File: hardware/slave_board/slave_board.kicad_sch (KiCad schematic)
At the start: 0 parts

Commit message: feat(hw): complete Root and Power_Stage schematic routing
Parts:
- added J1: RJ45_Shielded, symbol Connector:RJ45_Shielded
- added J2: Barrel_Jack_MountingPin, symbol Connector:Barrel_Jack_MountingPin
- added J3: Screw_Terminal_01x04, symbol Connector:Screw_Terminal_01x04
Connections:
- new net +12V: J2.1
- new net +3.3V: J1.3
- new net 1W_DATA: J1.8
- new net ADC_ALERT: J1.7
- new net FAN_PWM: J1.6
- new net GND: J1.2, J1.SH, J2.2
- new net I2C_SCL: J1.5
- new net I2C_SDA: J1.4
- new net LOAD_FORCE_+: J3.1 (Pin_1)
- new net LOAD_FORCE_-: J3.4 (Pin_4)
- new net LOAD_SENSE_+: J3.2 (Pin_2)
- new net LOAD_SENSE_-: J3.3 (Pin_3)
- new net PWM_IN: J1.1
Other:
- added sheet Power_Stage (power_stage.kicad_sch)
- added sheet Telemetry (telemetry.kicad_sch)

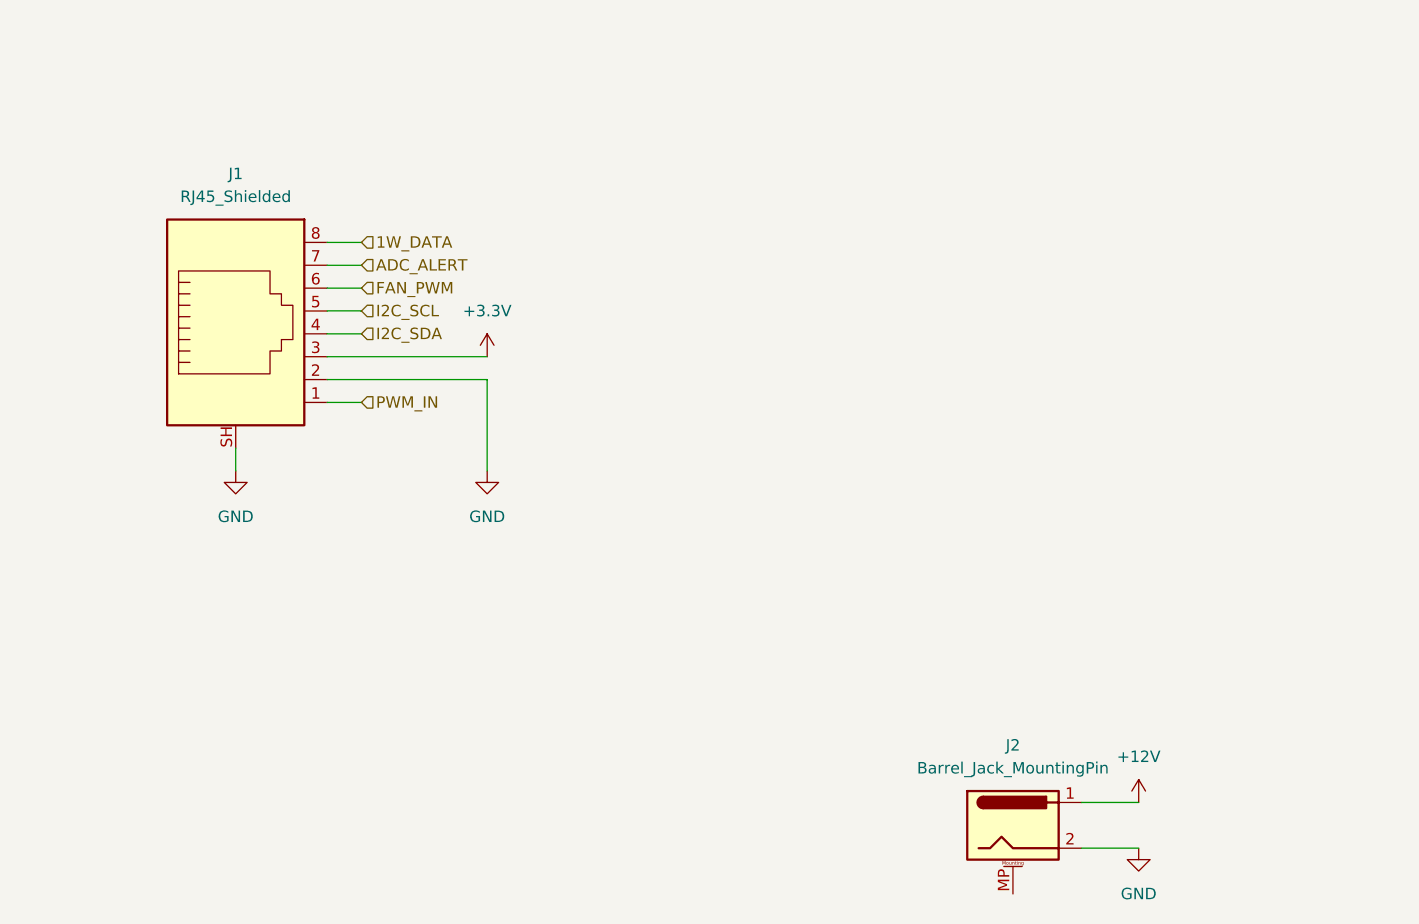
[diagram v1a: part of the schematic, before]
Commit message: feat(hw): add Master-board RJ45 protection circuit with PTC and BAT54S clamps
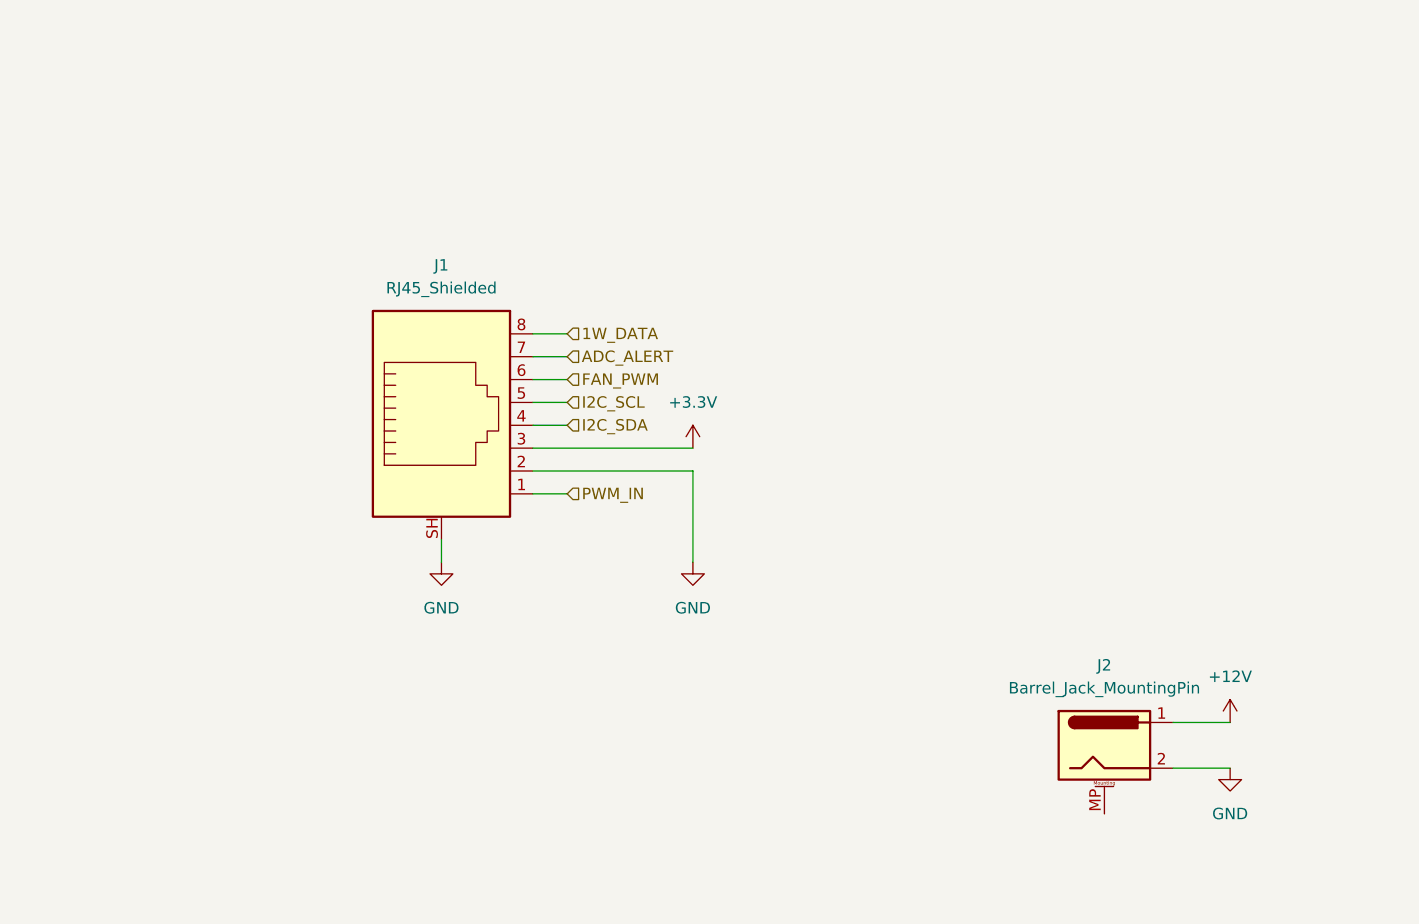
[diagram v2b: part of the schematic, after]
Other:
- moved on the sheet: J1, J2

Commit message: hw(slave): fix footprints, enforce HandSolder, defer connector selection
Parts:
- J2: footprint (none) -> Connector_BarrelJack:BarrelJack_Horizontal
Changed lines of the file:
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@@
 			)
 		)
-		(property "Footprint" ""
+		(property "Footprint" "Connector_BarrelJack:BarrelJack_Horizontal"
 			(at 142.24 144.526 0)
 			(hide yes)

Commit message: Implement cooling sheet, fan control, and update power connectors
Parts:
- removed J3: Screw_Terminal_01x04, symbol Connector:Screw_Terminal_01x04
- added F1: 25A, Fuse:Fuse_2920_7451Metric_Pad2.10x5.45mm_HandSolder, symbol Device:Fuse
- added J_PWR1: XT60PW-M, Connector_AMASS:AMASS_XT60PW-M_1x02_P7.20mm_Horizontal, symbol Connector_Generic:Conn_01x02
- added J_SENSE1: Micro-Fit 3.0 1x02, Connector_Molex:Molex_Micro-Fit_3.0_43650-0200_1x02_P3.00mm_Horizontal, symbol Connector_Generic:Conn_01x02
- added J_TEMP1: Micro-Fit 3.0 2x02, Connector_Molex:Molex_Micro-Fit_3.0_43045-0400_2x02_P3.00mm_Horizontal, symbol Connector_Generic:Conn_02x02_Odd_Even
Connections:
- net +3.3V: now also J_TEMP1.1 (Pin_1)
- net 1W_DATA: now also J_TEMP1.2 (Pin_2)
- net GND: now also J_TEMP1.3 (Pin_3)
- net LOAD_FORCE_+: now also F1.1
- net LOAD_FORCE_-: now also J_PWR1.2 (Pin_2)
- net LOAD_SENSE_+: now also J_SENSE1.1 (Pin_1)
- net LOAD_SENSE_-: now also J_SENSE1.2 (Pin_2)
- new net: F1.2, J_PWR1.1 (Pin_1)
- no-connect marks 0 -> 1
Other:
- added sheet cooling_thermal (cooling_thermal.kicad_sch)
